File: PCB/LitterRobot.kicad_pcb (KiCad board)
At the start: 4 copper layers, 55 x 140 mm, 31 parts, among them J1 DF11C-4DP-2V(57), J2 DF11C-6DP-2V(57), J3 DF11C-8DP-2V(57), J4 DF11C-6DP-2V(57), J5 TSM-105-01-S-DV, Q19 BC817, Q20 BC817, Q21 BC817, SW1 PCB_Push_Button, SW2 PCB_Push_Button, SW3 PCB_Push_Button, SW4 PCB_Push_Button, SW5 PCB_Push_Button, SW6 PCB_Push_Button, U3 VEML6035, U4 10CL016YE144C8G

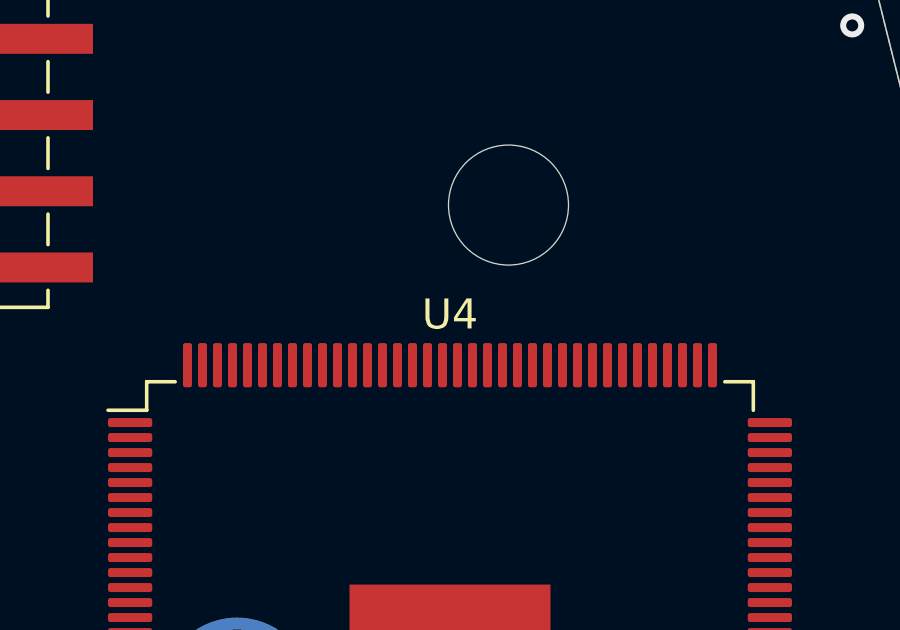
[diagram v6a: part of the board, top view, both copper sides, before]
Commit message: Add support for the hall sensors and dome LED
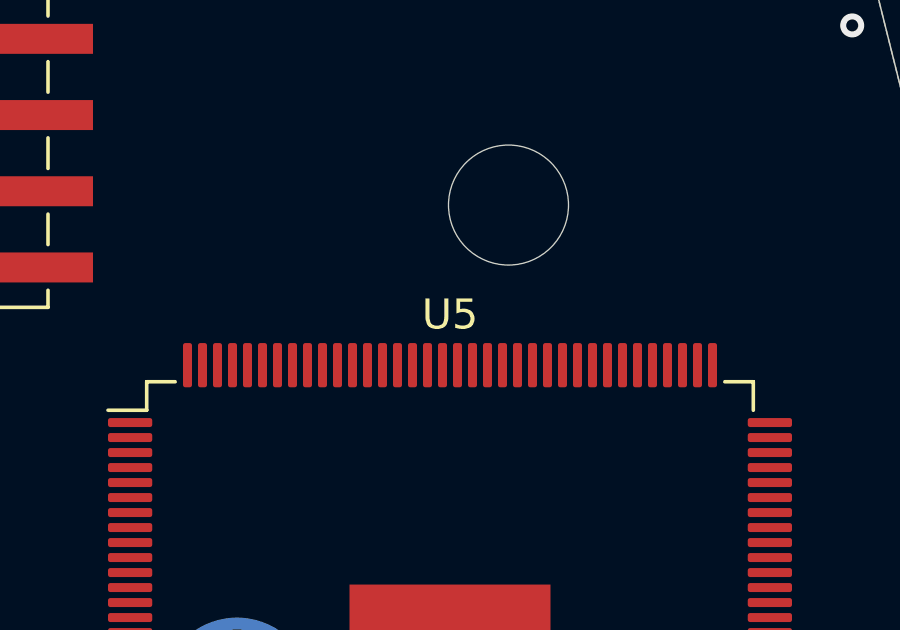
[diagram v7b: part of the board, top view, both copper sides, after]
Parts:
- renumbered U4 to U5
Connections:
- J3 pad 1: (no net) -> /Hall_sensor_VCC
- J3 pad 2: (no net) -> /Hall_sensor_L
- J3 pad 3: (no net) -> /Hall_sensor_R
- J3 pad 7: (no net) -> /Dome_LED_P
- J3 pad 8: (no net) -> /Dome_LED_N
- U5 pad 136: (no net) -> /FPGA/Hall_sensor_L
- U5 pad 137: (no net) -> /FPGA/Hall_sensor_R
- U5 pad 58: (no net) -> /Dome LED/Dome_LED

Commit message: Place all the components on the board
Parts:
- added C1: 22µF, Capacitor_SMD:C_1206_3216Metric, F.Cu at (88.5, 92.0)
- added C10: 100nF, Capacitor_SMD:C_0603_1608Metric, F.Cu at (87.0, 139.5)
- added C11: 100nF, Capacitor_SMD:C_0603_1608Metric, F.Cu at (97.5, 114.5)
- added C12: 100nF, Capacitor_SMD:C_0603_1608Metric, F.Cu at (84.0, 113.5)
- added C13: 100nF, Capacitor_SMD:C_0603_1608Metric, F.Cu at (92.0, 139.5)
- added C14: 100nF, Capacitor_SMD:C_0603_1608Metric, F.Cu at (71.5, 130.0)
- added C15: 100nF, Capacitor_SMD:C_0603_1608Metric, F.Cu at (82.0, 113.5)
- added C16: 100nF, Capacitor_SMD:C_0603_1608Metric, F.Cu at (78.5, 117.5)
- added C17: 100nF, Capacitor_SMD:C_0603_1608Metric, F.Cu at (78.5, 135.0)
- added C18: 100nF, Capacitor_SMD:C_0603_1608Metric, F.Cu at (101.0, 139.5)
- added C19: 100nF, Capacitor_SMD:C_0603_1608Metric, F.Cu at (105.5, 136.0)
- added C2: 22µF, Capacitor_SMD:C_1206_3216Metric, F.Cu at (88.5, 89.5)
- added C20: 100nF, Capacitor_SMD:C_0603_1608Metric, F.Cu at (105.5, 121.5)
- added C21: 100nF, Capacitor_SMD:C_0603_1608Metric, F.Cu at (102.5, 114.5)
- added C22: 100nF, Capacitor_SMD:C_0603_1608Metric, F.Cu at (94.0, 114.5)
- added C23: 100nF, Capacitor_SMD:C_0603_1608Metric, F.Cu at (86.0, 113.5)
- added C24: 100nF, Capacitor_SMD:C_0603_1608Metric, F.Cu at (105.5, 134.5)
- added C25: 100nF, Capacitor_SMD:C_0603_1608Metric, F.Cu at (105.5, 118.5)
- added C26: 100nF, Capacitor_SMD:C_0603_1608Metric, F.Cu at (107.5, 139.5)
- added C27: 47µF, Capacitor_SMD:C_1206_3216Metric, F.Cu at (106.7, 156.0)
- added C28: 47µF, Capacitor_SMD:C_1206_3216Metric, F.Cu at (108.9, 157.2)
- added C29: 100nF, Capacitor_SMD:C_0603_1608Metric, F.Cu at (104.8, 153.2)
- added C3: 22µF, Capacitor_SMD:C_1206_3216Metric, F.Cu at (95.0, 107.0)
- added C30: 1µF, Capacitor_SMD:C_0603_1608Metric, F.Cu at (70.5, 141.0)
- added C31: 1µF, Capacitor_SMD:C_0603_1608Metric, F.Cu at (70.5, 146.0)
- added C32: 100nF, Capacitor_SMD:C_0603_1608Metric, F.Cu at (87.5, 52.8)
- added C4: 22µF, Capacitor_SMD:C_1206_3216Metric, F.Cu at (89.0, 107.0)
- added C5: 22µF, Capacitor_SMD:C_1206_3216Metric, F.Cu at (85.5, 97.5)
- added C6: 22µF, Capacitor_SMD:C_1206_3216Metric, F.Cu at (98.5, 97.5)
- added C7: 1µF, Capacitor_SMD:C_0603_1608Metric, F.Cu at (96.0, 92.0)
- added C8: 100nF, Capacitor_SMD:C_0603_1608Metric, F.Cu at (79.5, 130.5)
- added C9: 100nF, Capacitor_SMD:C_0603_1608Metric, F.Cu at (105.5, 132.0)
- added D1: VS-2EYH02HM3/H, LitterRobot:Vishay_SlimSMAW, F.Cu at (84.0, 150.5)
- added D2: VS-2EYH02HM3/H, LitterRobot:Vishay_SlimSMAW, F.Cu at (94.5, 152.5)
- added D3: VS-2EYH02HM3/H, LitterRobot:Vishay_SlimSMAW, F.Cu at (107.5, 144.0)
- added F1: 1.1A, LitterRobot:Bel_Fuse_0ZCG, F.Cu at (91.0, 147.0)
- added JP1: Jumper, Jumper:SolderJumper-2_P1.3mm_Bridged_RoundedPad1.0x1.5mm, F.Cu at (92.5, 92.3)
- added Q1: BSS138, Package_TO_SOT_SMD:SOT-23, F.Cu at (78.5, 145.0)
- added Q10: BC817, Package_TO_SOT_SMD:SOT-23, F.Cu at (72.0, 69.5)
- added Q11: BC817, Package_TO_SOT_SMD:SOT-23, F.Cu at (72.0, 66.0)
- added Q12: BC817, Package_TO_SOT_SMD:SOT-23, F.Cu at (72.0, 62.5)
- added Q13: BC817, Package_TO_SOT_SMD:SOT-23, F.Cu at (72.0, 84.5)
- added Q14: BC817, Package_TO_SOT_SMD:SOT-23, F.Cu at (72.0, 81.0)
- added Q15: BC817, Package_TO_SOT_SMD:SOT-23, F.Cu at (72.0, 77.5)
- added Q16: BC817, Package_TO_SOT_SMD:SOT-23, F.Cu at (80.0, 69.5)
- added Q17: BC817, Package_TO_SOT_SMD:SOT-23, F.Cu at (80.0, 66.0)
- added Q18: BC817, Package_TO_SOT_SMD:SOT-23, F.Cu at (80.0, 62.5)
- added Q2: BSS138, Package_TO_SOT_SMD:SOT-23, F.Cu at (86.5, 145.0)
- added Q22: BC817, Package_TO_SOT_SMD:SOT-23, F.Cu at (84.0, 46.5)
- added Q23: BC817, Package_TO_SOT_SMD:SOT-23, F.Cu at (84.0, 43.0)
- added Q24: BC817, Package_TO_SOT_SMD:SOT-23, F.Cu at (84.0, 39.5)
- added Q3: BC817, Package_TO_SOT_SMD:SOT-23, F.Cu at (112.0, 150.0)
- added Q4: BC817, Package_TO_SOT_SMD:SOT-23, F.Cu at (72.0, 46.5)
- added Q5: BC817, Package_TO_SOT_SMD:SOT-23, F.Cu at (72.0, 43.0)
- added Q6: BC817, Package_TO_SOT_SMD:SOT-23, F.Cu at (72.0, 39.5)
- added Q7: BC817, Package_TO_SOT_SMD:SOT-23, F.Cu at (72.0, 58.0)
- added Q8: BC817, Package_TO_SOT_SMD:SOT-23, F.Cu at (72.0, 54.5)
- added Q9: BC817, Package_TO_SOT_SMD:SOT-23, F.Cu at (72.0, 51.0)
- added R1: 10k, Resistor_SMD:R_0603_1608Metric, F.Cu at (77.4, 161.0)
- added R10: 2.94k, Resistor_SMD:R_0603_1608Metric, F.Cu at (88.0, 94.0)
- added R11: 10k, Resistor_SMD:R_0603_1608Metric, F.Cu at (97.8, 102.0)
- added R12: 3.3k, Resistor_SMD:R_0603_1608Metric, F.Cu at (96.0, 95.5)
- added R13: 3.3k, Resistor_SMD:R_0603_1608Metric, F.Cu at (97.8, 100.5)
- added R14: 3.3k, Resistor_SMD:R_0603_1608Metric, F.Cu at (96.0, 94.0)
- added R15: 10k, Resistor_SMD:R_0603_1608Metric, F.Cu at (72.5, 124.5)
- added R16: 10k, Resistor_SMD:R_0603_1608Metric, F.Cu at (72.5, 123.0)
- added R17: 10k, Resistor_SMD:R_0603_1608Metric, F.Cu at (81.0, 98.0)
- added R18: 10k, Resistor_SMD:R_0603_1608Metric, F.Cu at (81.0, 93.0)
- added R19: 1k, Resistor_SMD:R_0603_1608Metric, F.Cu at (81.0, 100.5)
- added R2: 10k, Resistor_SMD:R_0603_1608Metric, F.Cu at (78.7, 161.7)
- added R20: 10k, Resistor_SMD:R_0603_1608Metric, F.Cu at (106.5, 126.0)
- added R21: 24.9, Resistor_SMD:R_0603_1608Metric, F.Cu at (72.5, 120.0)
- added R22: 10k, Resistor_SMD:R_0603_1608Metric, F.Cu at (104.5, 139.5)
- added R23: 28k, Resistor_SMD:R_0603_1608Metric, F.Cu at (100.5, 150.7)
- added R27: 10k, Resistor_SMD:R_0603_1608Metric, F.Cu at (84.0, 145.0)
- added R28: 3.3k, Resistor_SMD:R_0603_1608Metric, F.Cu at (86.0, 55.5)
- added R29: 3.3k, Resistor_SMD:R_0603_1608Metric, F.Cu at (86.0, 57.0)
- added R3: 20k, Resistor_SMD:R_0603_1608Metric, F.Cu at (97.0, 104.5)
- added R30: 3.3k, Resistor_SMD:R_0603_1608Metric, F.Cu at (86.0, 58.5)
- added R31: 178R, Resistor_SMD:R_0603_1608Metric, F.Cu at (112.0, 152.5)
- added R32: 10k, Resistor_SMD:R_0603_1608Metric, F.Cu at (78.0, 46.5)
- added R33: 10k, Resistor_SMD:R_0603_1608Metric, F.Cu at (78.0, 77.5)
- added R34: 10k, Resistor_SMD:R_0603_1608Metric, F.Cu at (81.0, 103.5)
- added R35: 10k, Resistor_SMD:R_0603_1608Metric, F.Cu at (78.5, 138.0)
- added R36: 178R, Resistor_SMD:R_0603_1608Metric, F.Cu at (69.5, 46.5)
- added R37: 221R, Resistor_SMD:R_0603_1608Metric, F.Cu at (69.5, 43.0)
- added R38: 221R, Resistor_SMD:R_0603_1608Metric, F.Cu at (69.5, 39.5)
- added R39: 178R, Resistor_SMD:R_0603_1608Metric, F.Cu at (69.5, 58.0)
- added R4: 1.87k, Resistor_SMD:R_0603_1608Metric, F.Cu at (98.5, 104.5)
- added R40: 221R, Resistor_SMD:R_0603_1608Metric, F.Cu at (69.5, 54.5)
- added R41: 221R, Resistor_SMD:R_0603_1608Metric, F.Cu at (69.5, 51.0)
- added R42: 178R, Resistor_SMD:R_0603_1608Metric, F.Cu at (69.5, 69.5)
- added R43: 221R, Resistor_SMD:R_0603_1608Metric, F.Cu at (69.5, 66.0)
- added R44: 221R, Resistor_SMD:R_0603_1608Metric, F.Cu at (69.5, 62.5)
- added R45: 178R, Resistor_SMD:R_0603_1608Metric, F.Cu at (69.5, 84.5)
- added R46: 221R, Resistor_SMD:R_0603_1608Metric, F.Cu at (69.5, 81.0)
- added R47: 221R, Resistor_SMD:R_0603_1608Metric, F.Cu at (69.5, 77.5)
- added R48: 178R, Resistor_SMD:R_0603_1608Metric, F.Cu at (77.5, 69.5)
- added R49: 221R, Resistor_SMD:R_0603_1608Metric, F.Cu at (77.5, 66.0)
- added R5: 11.5k, Resistor_SMD:R_0603_1608Metric, F.Cu at (87.0, 104.5)
- added R50: 221R, Resistor_SMD:R_0603_1608Metric, F.Cu at (77.5, 62.5)
- added R51: 178R, Resistor_SMD:R_0603_1608Metric, F.Cu at (77.5, 58.5)
- added R52: 221R, Resistor_SMD:R_0603_1608Metric, F.Cu at (77.5, 55.0)
- added R53: 221R, Resistor_SMD:R_0603_1608Metric, F.Cu at (77.5, 51.5)
- added R54: 178R, Resistor_SMD:R_0603_1608Metric, F.Cu at (81.5, 46.5)
- added R55: 221R, Resistor_SMD:R_0603_1608Metric, F.Cu at (81.5, 43.0)
- added R56: 221R, Resistor_SMD:R_0603_1608Metric, F.Cu at (81.5, 39.5)
- added R6: 10k, Resistor_SMD:R_0603_1608Metric, F.Cu at (86.2, 102.0)
- added R7: 10k, Resistor_SMD:R_0603_1608Metric, F.Cu at (86.2, 100.5)
- added R8: 2.55k, Resistor_SMD:R_0603_1608Metric, F.Cu at (85.5, 104.5)
- added R9: 9.31k, Resistor_SMD:R_0603_1608Metric, F.Cu at (88.0, 95.5)
- added TP1: TestPoint, TestPoint:TestPoint_Pad_D1.0mm, F.Cu at (78.0, 120.0)
- added TP2: TestPoint, TestPoint:TestPoint_Pad_D1.0mm, F.Cu at (78.0, 123.0)
- added TP3: TestPoint, TestPoint:TestPoint_Pad_D1.0mm, F.Cu at (78.0, 126.0)
- added U1: MPM54304GMN-0001, LitterRobot:MPS_MPM54304_LGA33_7x7mm, F.Cu at (92.0, 100.5)
- added U3: S25FL128SAGMFI000, Package_SO:SOIC-16W_7.5x10.3mm_P1.27mm, F.Cu at (74.8, 111.0)
- added U4: DRV8871DDA, Package_SO:Texas_HTSOP-8-1EP_3.9x4.9mm_P1.27mm_EP2.95x4.9mm_Mask2.4x3.1mm_ThermalVias, F.Cu at (104.4, 148.9)
- added U5: MCP1700T-5002E/TT, Package_TO_SOT_SMD:SOT-23, F.Cu at (70.5, 143.5)
- added X1: X1G0044510011, LitterRobot:Seiko_SG5032CAN, F.Cu at (75.5, 130.0)
- H1, H2, H3, H4, H5: moved to B.Cu
- R24: value 178R -> 10k
- R25, R26: value 221R -> 10k
- moved R26 100.9 mm to (86.5, 142.5), turned to 0 degrees
- moved R24 99.4 mm to (76.0, 145.0), turned to 270 degrees
- moved R25 96.8 mm to (78.5, 142.5), turned to 180 degrees
- moved Q19 15.4 mm to (80.0, 58.5), turned to 0 degrees
- moved Q21 15.3 mm to (80.0, 51.5)
- moved Q20 13.6 mm to (80.0, 55.0), turned to 0 degrees
- moved J5 10.0 mm to (73.2, 98.0), turned to 180 degrees
- moved U2 2.00 mm to (92.0, 127.0)
- renumbered D2 to D10, D7 to D4, D4 to D5, D5 to D7, D1 to D8, D3 to D9, SW2 to SW1, SW3 to SW2, SW4 to SW3, SW1 to SW4, U5 to U2, U3 to U6
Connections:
- D4 pad 4: Net-(D7-Pad4) (its old number) -> Net-(D4-Pad4)
- D4 pad 5: Net-(D7-Pad5) (its old number) -> Net-(D4-Pad5)
- D4 pad 6: Net-(D7-Pad6) (its old number) -> Net-(D4-Pad6)
- D9 pad 4: Net-(D3-Pad4) -> Net-(D9-Pad4)
- D9 pad 5: Net-(D3-Pad5) -> Net-(D9-Pad5)
- D9 pad 6: Net-(D3-Pad6) -> Net-(D9-Pad6)
- Q19 pad 1: /Control panel/Power_LED_G -> /Control panel/Center_LED_G
- Q19 pad 3: Net-(D7-Pad4) (its old number) -> Net-(D9-Pad4)
- Q20 pad 1: /FPGA/Power_LED_B -> /Control panel/Center_LED_R
- Q20 pad 3: Net-(D7-Pad5) (its old number) -> Net-(D9-Pad5)
- Q21 pad 1: /Control panel/Power_LED_B -> /Control panel/Center_LED_B
- Q21 pad 3: Net-(D7-Pad6) (its old number) -> Net-(D9-Pad6)
- R24 pad 1: Net-(Q19-Pad2) -> /Hall_sensor_VCC
- R24 pad 2: GND -> /Hall_sensor_L
- R25 pad 1: Net-(Q20-Pad2) -> +3V3
- R25 pad 2: GND -> /FPGA/Hall_sensor_L
- R26 pad 1: Net-(Q21-Pad2) -> /Hall_sensor_VCC
- R26 pad 2: GND -> /Hall_sensor_R
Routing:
- net /Reset_button: vias 2 -> 0
- net /Power_button: vias 1 -> 0
- net /Empty_button: vias 1 -> 0
- net /Cycle_button: vias 2 -> 0
